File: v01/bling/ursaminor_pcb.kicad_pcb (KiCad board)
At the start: 2 copper layers, 298.8 x 122 mm, 233 parts, among them J1 USB_C_Receptacle_USB2.0, J2 I2C-L, J3 I2C-R, J4 AVR-ISP-6, SW1 Reset, U1 ATmega32U4-AU, U2 MCP23017_SO, U3 IS31FL3733-TQ, U4 HOLE, U4 IS31FL3733-TQ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

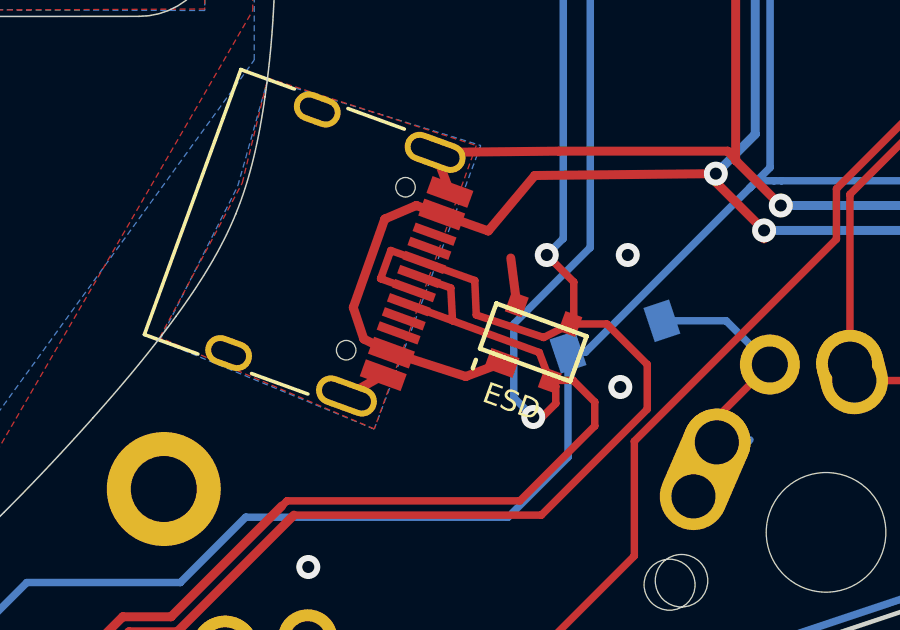
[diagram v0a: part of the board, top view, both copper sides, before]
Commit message: Fix incorrectly wired ESD
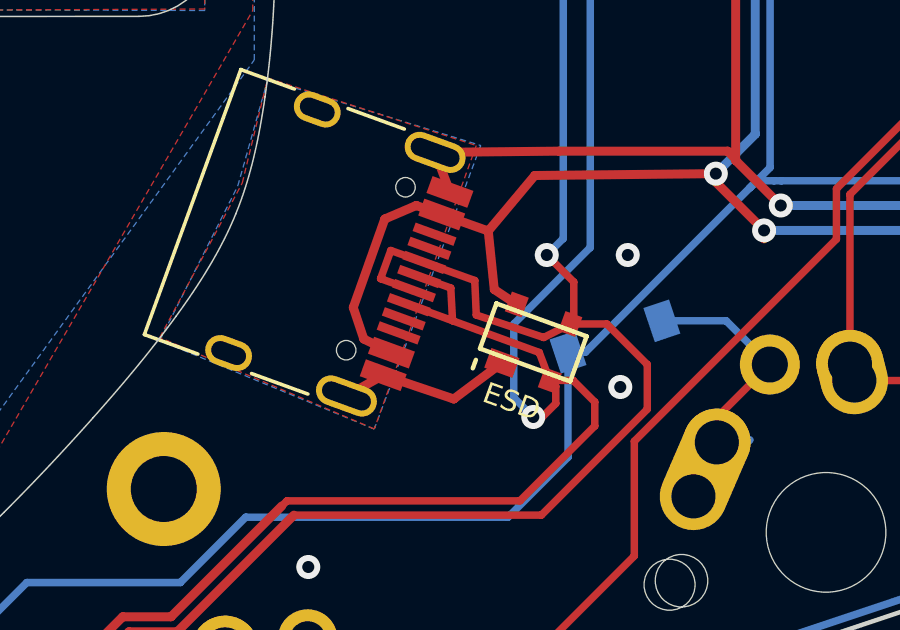
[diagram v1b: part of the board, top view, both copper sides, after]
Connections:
- U7 pad 1: VBUS -> VSS
- U7 pad 4: VSS -> VBUS
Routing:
- net VSS: track 147.8 -> 150.8 mm
- net VBUS: track 226.8 -> 225.8 mm

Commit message: Remove mounting holes as they didn't end up working
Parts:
- removed the REF** at (177.5, 110.4)
- removed the REF** at (198.4, 25.1)
- removed the REF** at (128.0, 25.2)
- removed the REF** at (255.8, 106.1)
- removed the REF** at (71.0, 106.1)
- removed the REF** at (293.5, 24.9)
- removed the REF** at (32.9, 24.8)
- removed the REF** at (149.1, 110.3)
